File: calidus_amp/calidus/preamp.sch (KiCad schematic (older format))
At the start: 30 parts, among them U8 OPA2134

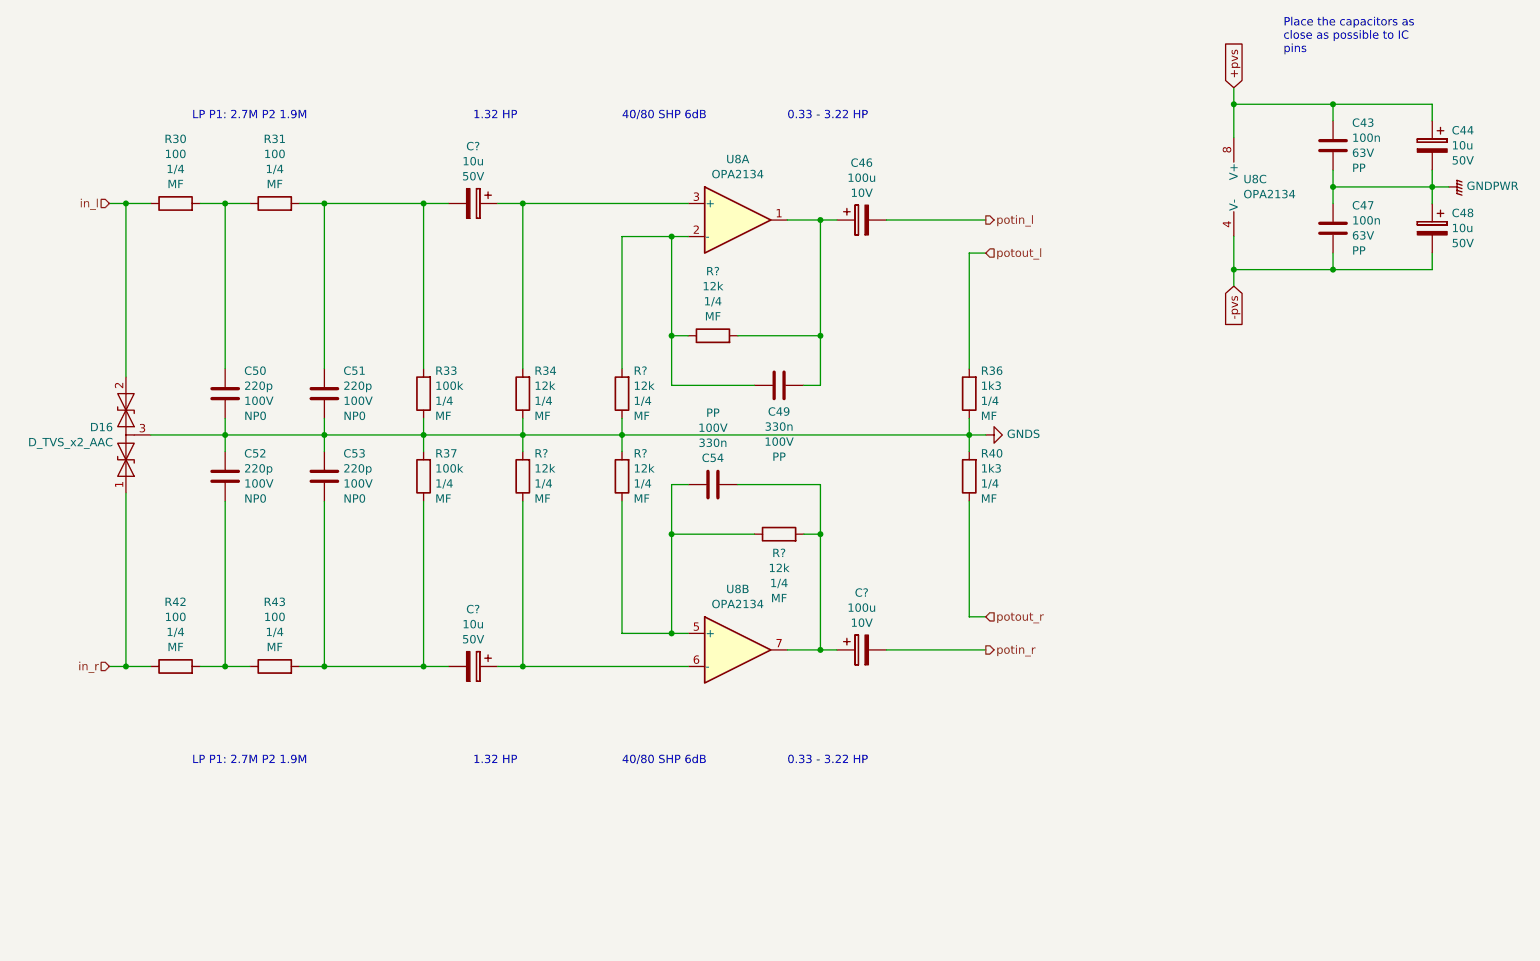
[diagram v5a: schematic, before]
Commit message: WIP: component footprint assignment.
Signed-off-by: Nenad Radulovic <nenad.b.radulovic@gmail.com>
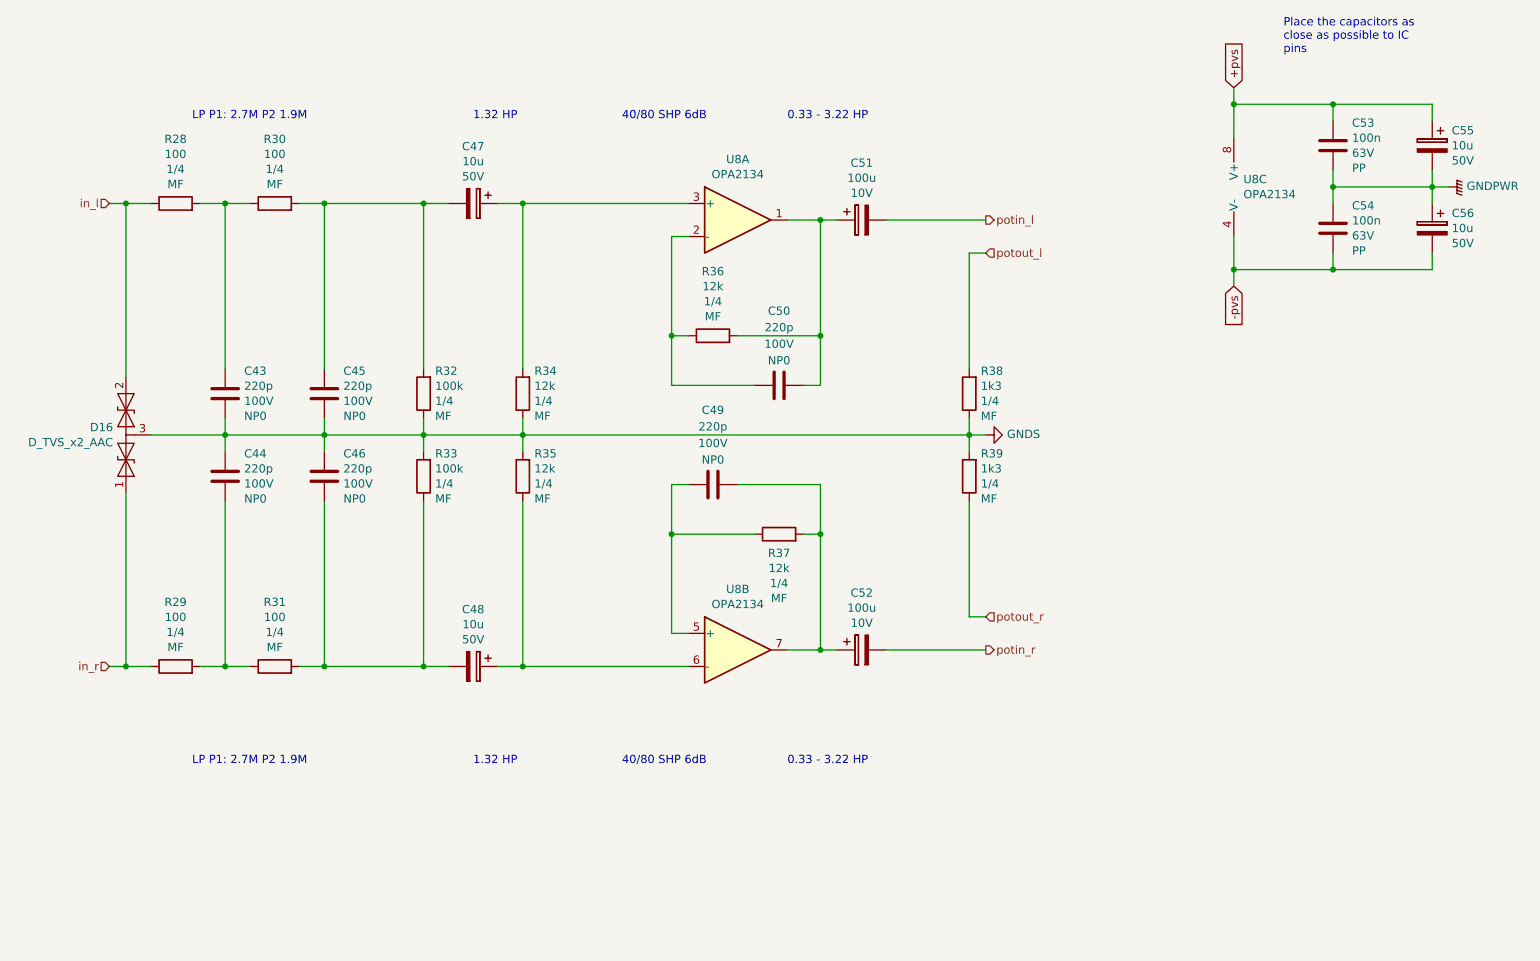
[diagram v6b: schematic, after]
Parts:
- removed C54: 330n, symbol Device:C
- removed R? (x2): 12k, symbol Device:R
- added C50: 220p, Capacitor_THT:C_Disc_D3.0mm_W2.0mm_P2.50mm, symbol Device:C
- C43: renamed from C50; footprint (none) -> Capacitor_THT:C_Disc_D3.0mm_W2.0mm_P2.50mm
- C44: renamed from C52; footprint (none) -> Capacitor_THT:C_Disc_D3.0mm_W2.0mm_P2.50mm
- C45: renamed from C51; footprint (none) -> Capacitor_THT:C_Disc_D3.0mm_W2.0mm_P2.50mm
- C46: renamed from C53; footprint (none) -> Capacitor_THT:C_Disc_D3.0mm_W2.0mm_P2.50mm
- C49: value 330n -> 220p; footprint (none) -> Capacitor_THT:C_Disc_D3.0mm_W2.0mm_P2.50mm; Type PP -> NP0
- C53: renamed from C43; footprint (none) -> Capacitor_THT:C_Rect_L7.0mm_W2.5mm_P5.00mm
- C54: renamed from C47; footprint (none) -> Capacitor_THT:C_Rect_L7.0mm_W2.5mm_P5.00mm
- D16: footprint (none) -> Diode_SMD:D_Powermite3
- R28: renamed from R30; footprint (none) -> Resistor_THT:R_Axial_DIN0207_L6.3mm_D2.5mm_P7.62mm_Horizontal
- R29: renamed from R42; footprint (none) -> Resistor_THT:R_Axial_DIN0207_L6.3mm_D2.5mm_P7.62mm_Horizontal
- R30: renamed from R31; footprint (none) -> Resistor_THT:R_Axial_DIN0207_L6.3mm_D2.5mm_P7.62mm_Horizontal
- R31: renamed from R43; footprint (none) -> Resistor_THT:R_Axial_DIN0207_L6.3mm_D2.5mm_P7.62mm_Horizontal
- R32: renamed from R33; footprint (none) -> Resistor_THT:R_Axial_DIN0207_L6.3mm_D2.5mm_P7.62mm_Horizontal
- R33: renamed from R37; footprint (none) -> Resistor_THT:R_Axial_DIN0207_L6.3mm_D2.5mm_P7.62mm_Horizontal
- R34: footprint (none) -> Resistor_THT:R_Axial_DIN0207_L6.3mm_D2.5mm_P7.62mm_Horizontal
- R35, R36, R37: renamed from R?; footprint (none) -> Resistor_THT:R_Axial_DIN0207_L6.3mm_D2.5mm_P7.62mm_Horizontal
- R38: renamed from R36; footprint (none) -> Resistor_THT:R_Axial_DIN0207_L6.3mm_D2.5mm_P7.62mm_Horizontal
- R39: renamed from R40; footprint (none) -> Resistor_THT:R_Axial_DIN0207_L6.3mm_D2.5mm_P7.62mm_Horizontal
- gave numbers to parts that had none: 3
- renumbered C46 to C51, C44 to C55, C48 to C56
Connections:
- net at C51.1, R36.2, U8.1: now also C50.1; no longer C49.1
- net at R36.1, U8.2 (-): now also C50.2; no longer C49.2
- net at C52.1, R37.2, U8.7: now also C49.1
- net at R37.1, U8.5 (+): now also C49.2
